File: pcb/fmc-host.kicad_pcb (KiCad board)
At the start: 6 copper layers, 76.5 x 339.8 mm, 309 parts, among them J1 SMA002, J10 BM08B-SURS-TF, J2 SMA002, J3 SMA002, J4 SMA002, J5 SMA002, J6 FTSH-105-01-F-D-RA-K, J7 12226-8250-00FR, J8 FMC_SINGLE_WIDTH_MODULE, J9 ASP-134488-01, Q1 SI1012R, Q2 SI1012R, U1 SN74LVC2G34DCKR, U10 DS90UB934-Q1, U11 DS91M040, U12 AD5766BCPZ-RL7, U13 MCP47FEB02A0-E/ST, U14 LM4132AMF-2.5/NOPBCT-ND, U15 AD7616BSTZ, U16 AD5142BCPZ10, U17 LTM4622A, U18 D3V3XA4B10LP, U19 TPS7A49, U2 SN65LVDS9638DGN, U20 TPS7A49, U21 TPS7A30, U22 24ST, U23 LTM8049_BGA, U24 TPS62061DSGT, U25 D3V3XA4B10LP, U26 D3V3XA4B10LP, U3 FIN1032MTCX, U4 ADCMP600, U5 ADCMP600, U6 DG1412E, U7 DG1412E, U8 DG1412E, U9 DS90UB934-Q1, X2 OE-LOGO_7X5

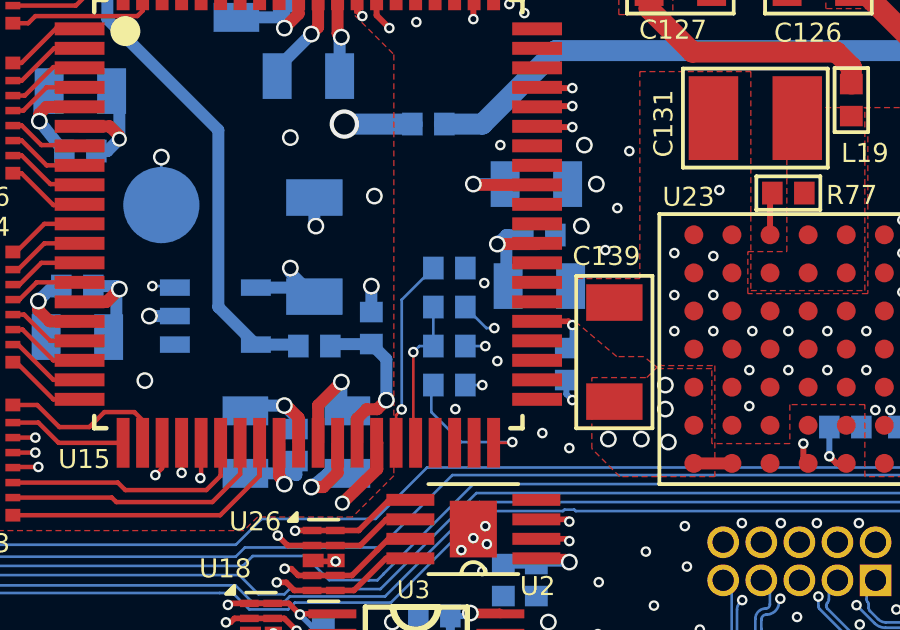
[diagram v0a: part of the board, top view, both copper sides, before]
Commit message: Fix AD761x nRESET input
- Replace 0.1uF filter capacitor with 100pF
- Replace series 10k resistor with 0 ohm jumper
- Add 10k pulldown so that chip power-on defaults to the reset state
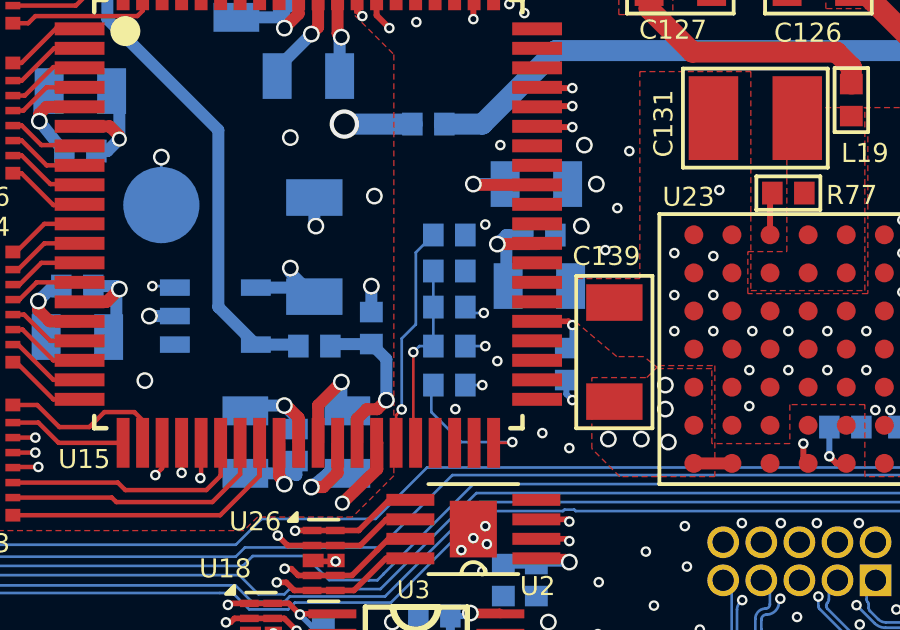
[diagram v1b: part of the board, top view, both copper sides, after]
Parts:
- added R82: 10k, fmc-host:0402, B.Cu at (145.4, 229.6)
- C115: value 0.1uF -> 100pF
- R66: value 10k -> 0
- moved R63 1.10 mm to (145.4, 228.4)
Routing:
- net Net-(U15-~{RESET}): track 5.11 -> 6.26 mm
- net Net-(U15-REFSEL): track 7.14 -> 8.24 mm
